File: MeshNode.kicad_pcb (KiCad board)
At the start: 2 copper layers, 75.4 x 52.8 mm, 31 parts, among them J1 MicroSD_Module, J2 AHT20+BMP280, J3 Solar, J4 Battery, J5 I2C pins, Q1 IRLZ44N, U3 MIC5219-3.3YM5

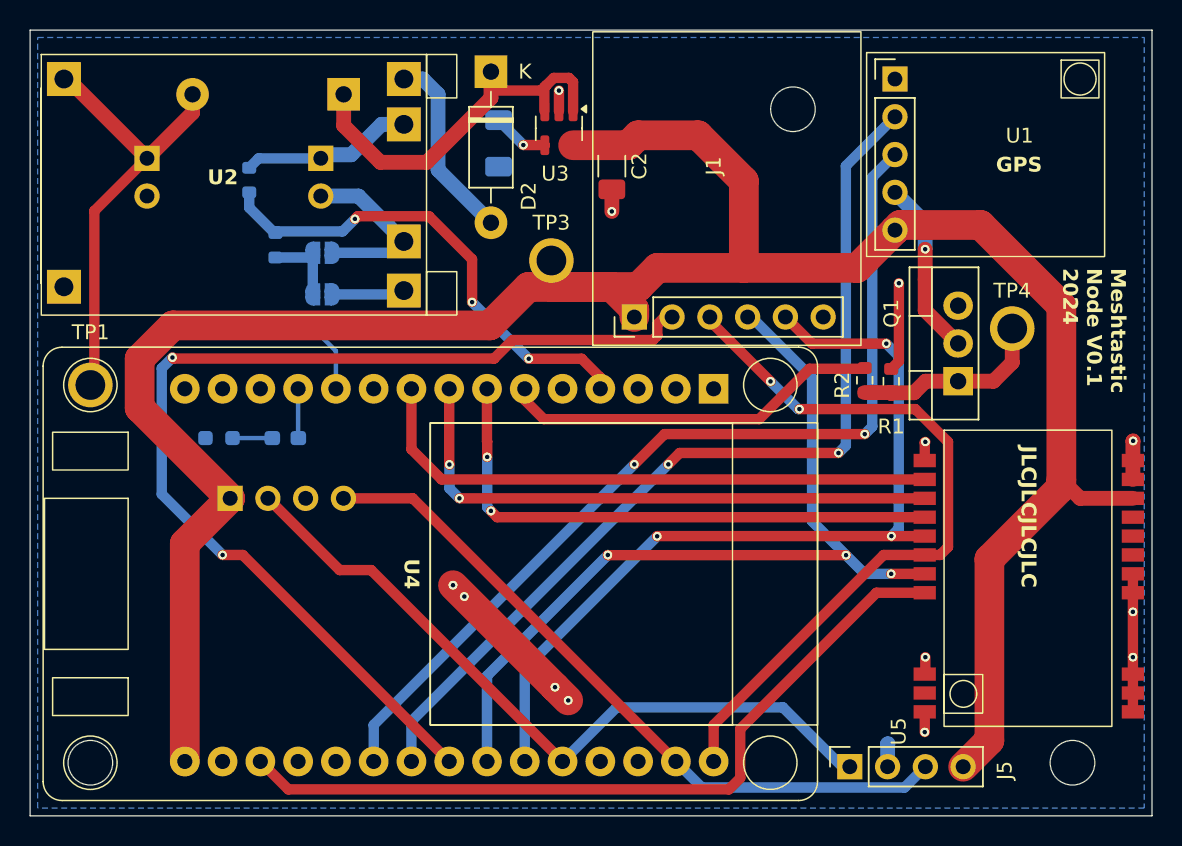
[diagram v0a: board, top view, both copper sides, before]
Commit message: Changed FET, resized traces, connected S22 connections
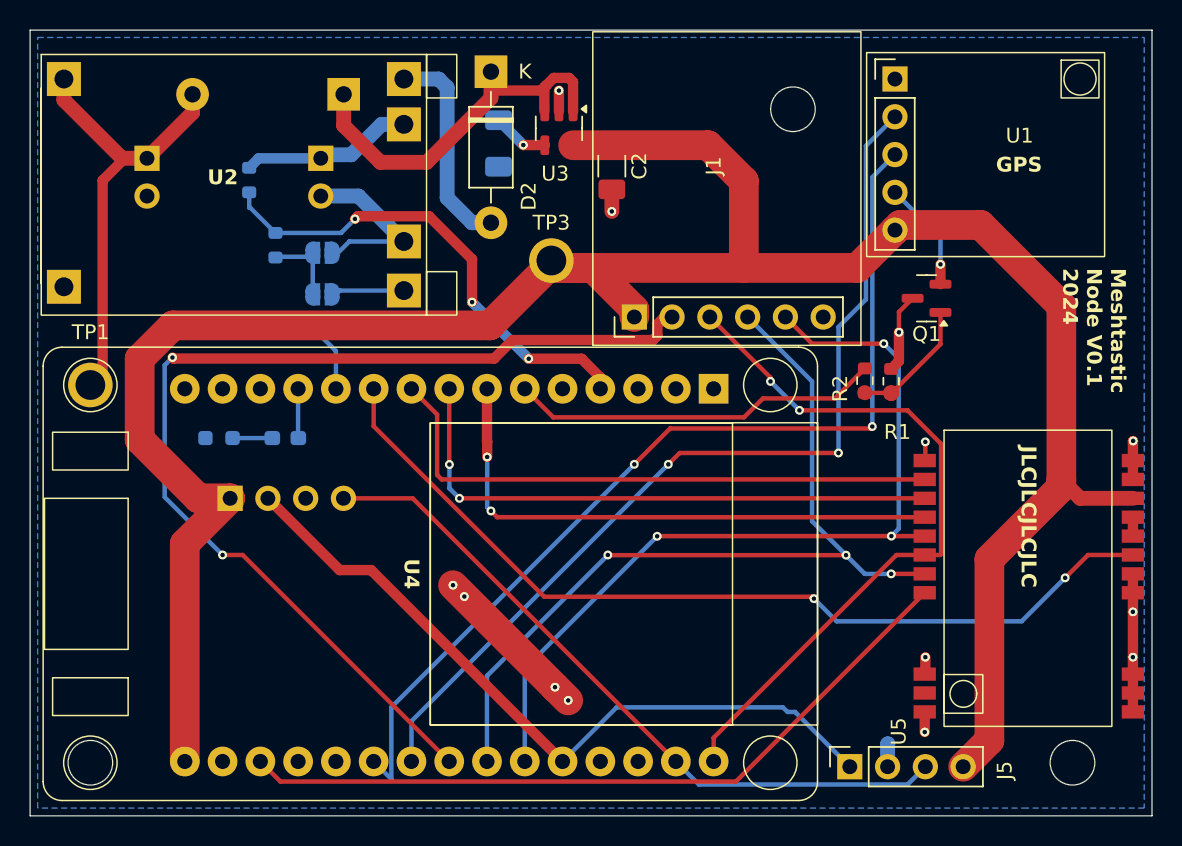
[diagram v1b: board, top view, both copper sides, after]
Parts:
- removed TP4: GPS, TestPoint:TestPoint_Plated_Hole_D2.0mm
- Q1: value IRLZ44N -> IRLML6344; footprint Package_TO_SOT_THT:TO-220-3_Vertical -> Package_TO_SOT_SMD:SOT-23
- moved Q1 5.97 mm to (142.1, 84.6), turned to 180 degrees
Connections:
- U4 pad 10: unconnected-(U4-D27-Pad10) -> LORA_RXEN
- U5 pad 16: LORA_TXEN -> LORA_DIO2
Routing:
- net LORA_RXEN: track 0.00 -> 60.9 mm, vias 0 -> 2
- net Net-(Q1-D): track 11.9 -> 7.44 mm
- net Net-(Q1-G): track 13.1 -> 8.76 mm
- net GPS_TX: track 63.2 -> 65.6 mm
- net SPI_CS_LORA: track 52.9 -> 50.5 mm
- net SOLAR: track 30.2 -> 31.9 mm
- net 3V3: track 163.5 -> 164.9 mm
- net +5V: track 12.8 -> 14.2 mm
- net LORA_DIO2: track 0.00 -> 1.27 mm
- net SPI_MOSI: track 49.9 -> 48.6 mm
- net GND: track 42.0 -> 41.3 mm
